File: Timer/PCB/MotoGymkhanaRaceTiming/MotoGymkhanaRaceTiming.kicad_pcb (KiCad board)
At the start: 2 copper layers, 99.1 x 64.8 mm, 42 parts, among them U1 LM2577T-ADJ_NOPB, U2 PC817, U3 PC817

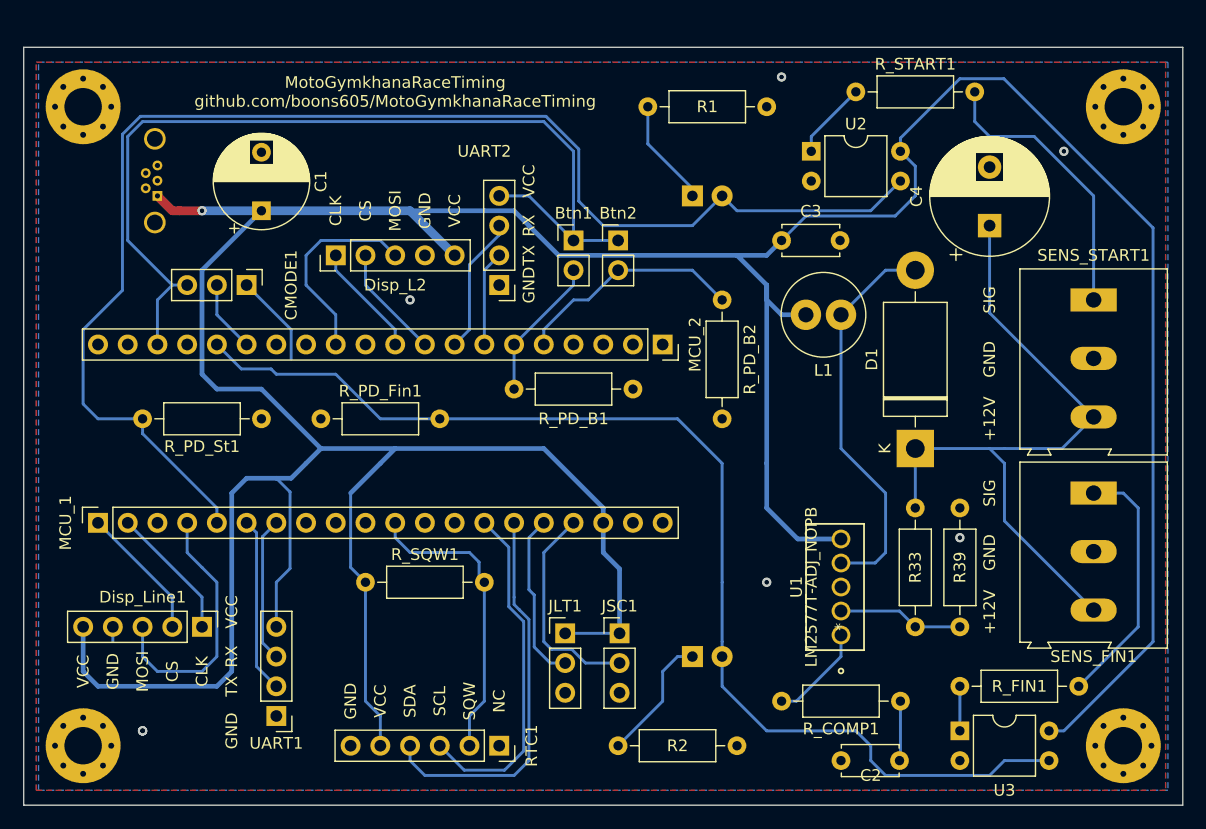
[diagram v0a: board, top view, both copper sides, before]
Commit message: Starting issue #29: Carrier PCB for central unit and improved PCBs for other units, as ordered.
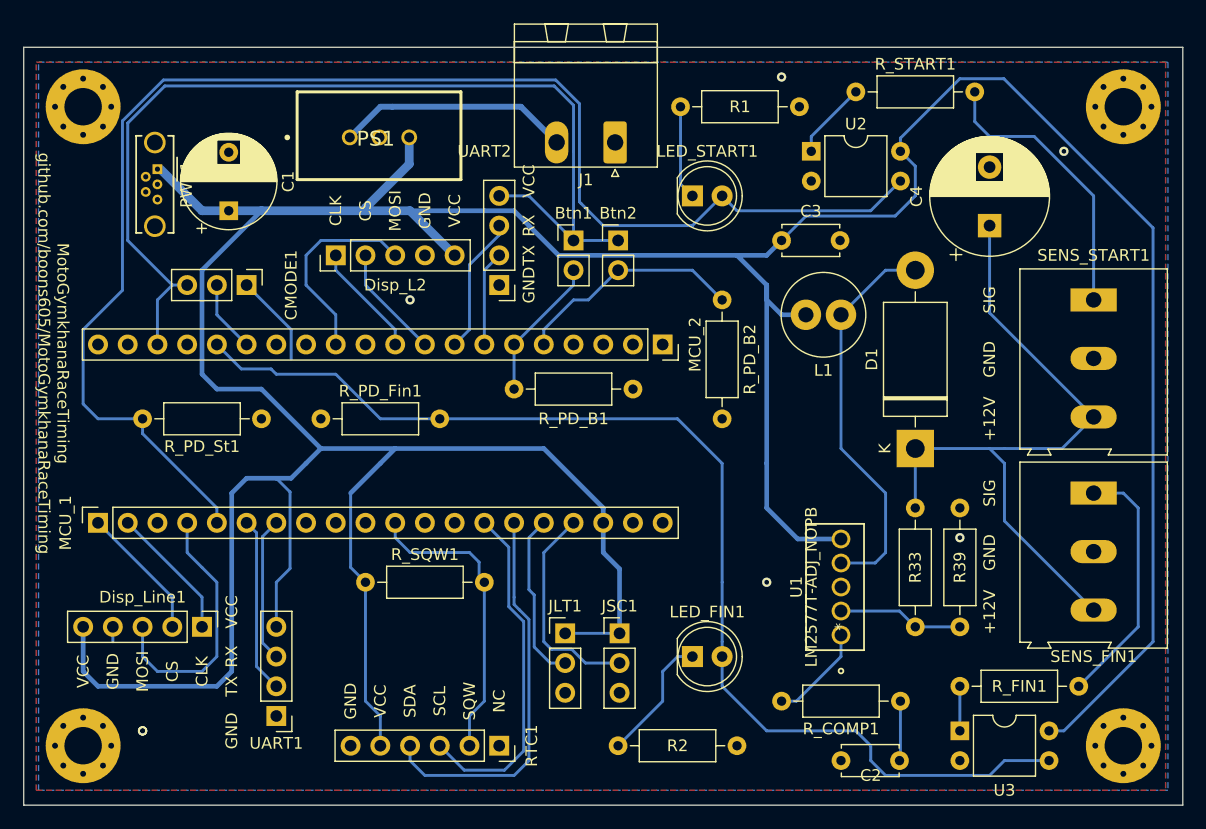
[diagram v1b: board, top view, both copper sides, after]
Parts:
- added J1: Screw_Terminal_01x02, Connector_Phoenix_MSTB:PhoenixContact_MSTBA_2,5_2-G_1x02_P5.00mm_Horizontal, F.Cu at (84.8, 34.8)
- added PS1: TSR_2-2450, MotoGymkhanaRaceTiming:TSR-2, F.Cu at (57.7, 30.5)
- LED_FIN1, LED_START1, PWR1: moved to F.Cu
- moved C1 2.79 mm to (51.8, 40.6)
- moved R1 2.79 mm to (100.6, 31.8)
- moved PWR1 2.29 mm to (45.7, 37.1), turned to 270 degrees
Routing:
- net Net-(J1-Pad2): track 0.00 -> 20.0 mm
- net +5V: track 346.6 -> 355.4 mm, vias 1 -> 0
- net Net-(LED_START1-Pad2): track 117.8 -> 123.3 mm
- net Net-(Btn1-Pad1): track 80.2 -> 85.7 mm
- net Net-(LED_START1-Pad1): track 9.17 -> 8.20 mm
